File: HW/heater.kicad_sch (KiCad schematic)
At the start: 14 parts, among them J1 Heater, Q1 RQ3E110AJ

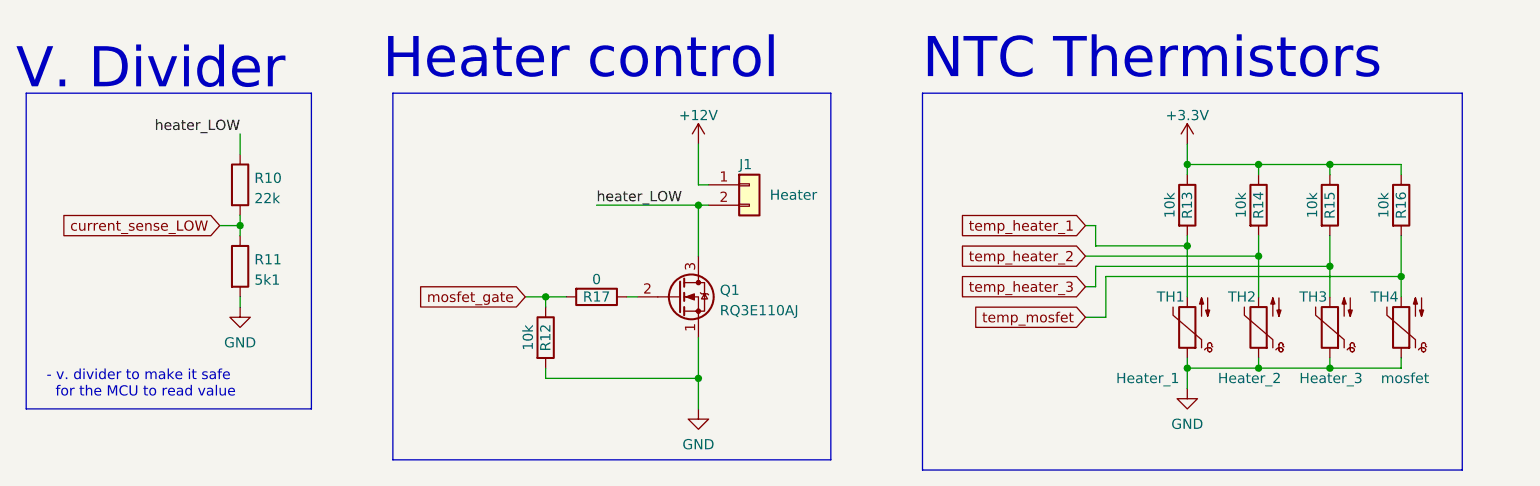
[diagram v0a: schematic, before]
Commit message: Fixed silkscreen, removed one thermistor, fixed component placement
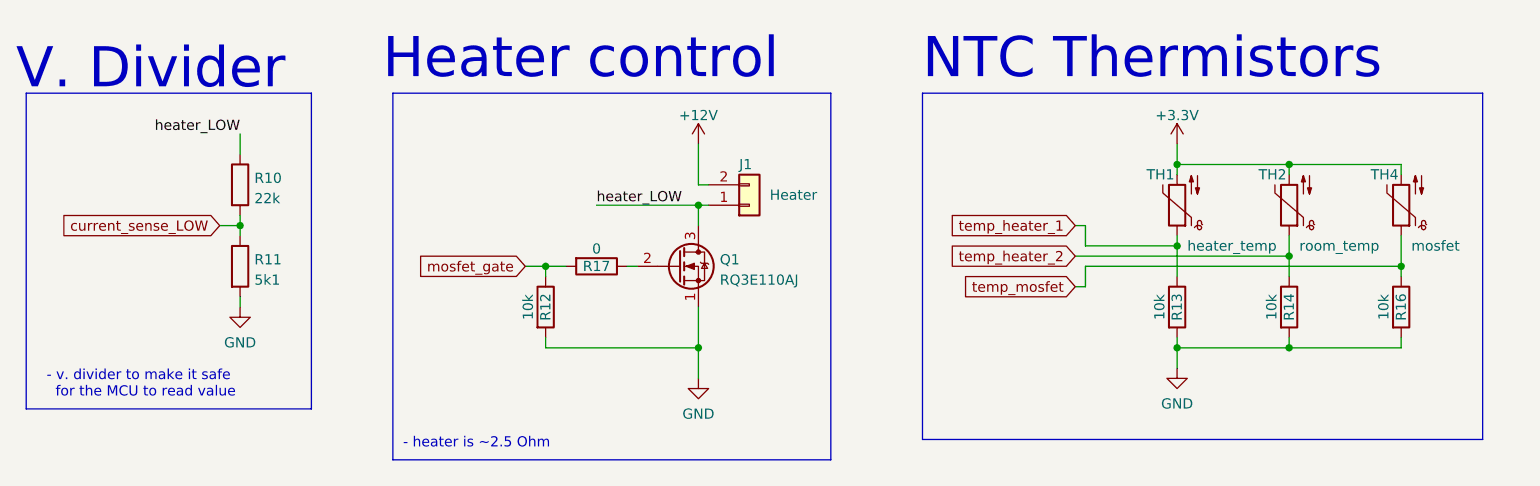
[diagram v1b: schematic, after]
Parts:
- removed R15: 10k, Resistor_SMD:R_0603_1608Metric, symbol Device:R
- removed TH3: Heater_3, Jumper:SolderJumper-2_P1.3mm_Open_RoundedPad1.0x1.5mm, symbol Device:Thermistor_NTC
- TH1: value Heater_1 -> heater_temp
- TH2: value Heater_2 -> room_temp
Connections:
- net +12V: now also J1.2 (Pin_2); no longer J1.1 (Pin_1)
- net +3V3: now also TH1.2, TH2.2, TH4.2; no longer R13.1, R14.1, R16.1
- net GND: now also R13.2, R14.2, R16.2; no longer TH1.1, TH2.1, TH4.1
- net heater_LOW: now also J1.1 (Pin_1); no longer J1.2 (Pin_2)
- net temp_heater_1: now also R13.1, TH1.1; no longer R13.2, TH1.2
- net temp_heater_2: now also R14.1, TH2.1; no longer R14.2, TH2.2
- net temp_mosfet: now also R16.1, TH4.1; no longer R16.2, TH4.2
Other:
- note added: "- heater is ~2.5 Ohm"
- moved on the sheet: Q1, R12, R13, R14, R16, R17, TH1, TH2, TH4

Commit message: Fixed component placement, enlarged some pcb slots, removed two thermistors
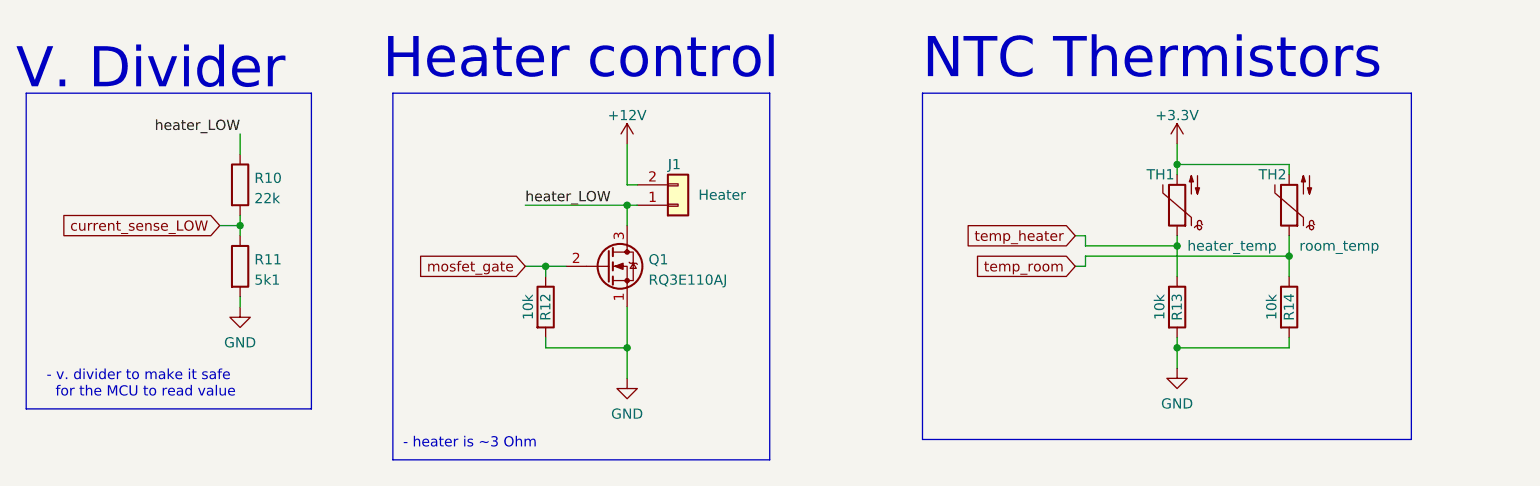
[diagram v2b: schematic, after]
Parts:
- removed R16: 10k, Resistor_SMD:R_0603_1608Metric, symbol Device:R
- removed R17: 0, Resistor_SMD:R_0603_1608Metric, symbol Device:R
- removed TH4: mosfet, Jumper:SolderJumper-2_P1.3mm_Open_RoundedPad1.0x1.5mm, symbol Device:Thermistor_NTC
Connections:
- net mosfet_gate: now also Q1.2 (G)
- net temp_heater_1 renamed temp_heater
- net temp_heater_2 renamed temp_room
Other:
- note added: "- heater is ~3 Ohm"
- note removed: "- heater is ~2.5 Ohm"
- moved on the sheet: J1, Q1
